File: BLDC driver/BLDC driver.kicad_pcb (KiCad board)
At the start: 4 copper layers, 75 x 50 mm, 41 parts, among them J1 Screw_Terminal_01x02, J2 Screw_Terminal_01x03, J3 Conn_02x06_Counter_Clockwise, J4 Izlaz ocitavanje struje, Q1 N0436N, Q2 N0436N, Q3 N0436N, Q4 N0436N, Q5 N0436N, Q6 N0436N, U1 MCP8027T-H/Y4X

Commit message: Ispravljene greske
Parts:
- moved J3 0.29 mm to (126.0, 74.1)
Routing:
- net PWM2L: track 15.5 -> 14.2 mm
- net I_OUT3: track 22.4 -> 23.3 mm
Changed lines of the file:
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@@
 			(at 3.75 -6.25 0)
 			(layer "F.SilkS")
+			(hide yes)
 			(effects
 				(font
@@
 			(at 3.75 6.25 0)
 			(layer "F.Fab")
+			(hide yes)
 			(effects
 				(font
@@
 	(footprint "Connector_PinHeader_2.54mm:PinHeader_2x06_P2.54mm_Vertical"
 		(layer "F.Cu")
-		(at 125.71 74.13)
+		(at 126 74.126511)
 		(descr "Through hole straight pin header, 2x06, 2.54mm pitch, double rows")
 		(tags "Through hole pin header THT 2x06 2.54mm double row")
@@
 			(at 1.27 -2.38 0)
 			(layer "F.SilkS")
+			(hide yes)
 			(effects
 				(font
@@
 			(at 1.27 15.08 0)
 			(layer "F.Fab")
+			(hide yes)
 			(effects
 				(font
@@
 	)
 	(segment
-		(start 128.25 81)
-		(end 132.314799 76.935201)
+		(start 129.691 80.595511)
+		(end 129.691 79.342479)
 		(width 0.2)
 		(layer "In2.Cu")
@@
 	)
 	(segment
-		(start 128.25 81.75)
-		(end 128.25 81)
+		(start 129.691 79.342479)
+		(end 132.314799 76.71868)
 		(width 0.2)
 		(layer "In2.Cu")
@@
 	)
 	(segment
+		(start 128.54 81.746511)
+		(end 128.387228 81.746511)
+		(width 0.2)
+		(layer "In2.Cu")
+		(net 36)
+	)
+	(segment
+		(start 128.387228 81.746511)
+		(end 128.25 81.609283)
+		(width 0.2)
+		(layer "In2.Cu")
+		(net 36)
+	)
+	(segment
+		(start 128.54 81.746511)
+		(end 129.691 80.595511)
+		(width 0.2)
+		(layer "In2.Cu")
+		(net 36)
+	)
+	(segment
 		(start 133 82.3375)
 		(end 133.4125 82.3375)
@@
 	)
 	(segment
-		(start 125.71 81.75)
-		(end 126.861 80.599)
+		(start 128.182489 77.817511)
+		(end 130.366025 77.817511)
 		(width 0.2)
 		(layer "In2.Cu")
@@
 	)
 	(segment
-		(start 126.861 78.97124)
-		(end 128.01124 77.821)
+		(start 127.389 78.611)
+		(end 128.182489 77.817511)
 		(width 0.2)
 		(layer "In2.Cu")
@@
 	)
 	(segment
-		(start 130.362536 77.821)
-		(end 136.082536 72.101)
+		(start 126 81.746511)
+		(end 127.389 80.357511)
 		(width 0.2)
 		(layer "In2.Cu")
@@
 	)
 	(segment
-		(start 128.01124 77.821)
-		(end 130.362536 77.821)
+		(start 136.082536 72.101)
+		(end 139.899 72.101)
 		(width 0.2)
 		(layer "In2.Cu")
@@
 	)
 	(segment
-		(start 126.861 80.599)
-		(end 126.861 78.97124)
+		(start 126 81.746511)
+		(end 126 81.46)
 		(width 0.2)
 		(layer "In2.Cu")
@@
 	)
 	(segment
-		(start 136.082536 72.101)
-		(end 139.899 72.101)
+		(start 127.389 80.357511)
+		(end 127.389 78.611)
+		(width 0.2)
+		(layer "In2.Cu")
+		(net 38)
+	)
+	(segment
+		(start 130.366025 77.817511)
+		(end 136.082536 72.101)
 		(width 0.2)
 		(layer "In2.Cu")
@@
 	)
 	(segment
-		(start 132.883212 78.3375)
-		(end 132.883212 77.25)
+		(start 134.75 79.5)
+		(end 133.558212 79.5)
 		(width 0.2)
 		(layer "F.Cu")
@@
 	)
 	(segment
-		(start 134.75 79.5)
-		(end 133.558212 79.5)
+		(start 132.883212 78.825)
+		(end 132.883212 78.3375)
 		(width 0.2)
 		(layer "F.Cu")
@@
 	)
 	(segment
-		(start 132.883212 78.825)
-		(end 132.883212 78.3375)
+		(start 132.883212 78.3375)
+		(end 132.883212 77.866788)
+		(width 0.2)
+		(layer "F.Cu")
+		(net 43)
+	)
+	(segment
+		(start 132.883212 77.866788)
+		(end 133.5 77.25)
 		(width 0.2)
 		(layer "F.Cu")
@@
 	)
 	(via
-		(at 132.883212 77.25)
+		(at 133.5 77.25)
 		(size 0.6)
 		(drill 0.3)
@@
 	)
 	(segment
+		(start 133.5 77.25)
+		(end 132.633212 77.25)
+		(width 0.2)
+		(layer "In2.Cu")
+		(net 43)
+	)
+	(segment
 		(start 132.633212 77.25)
 		(end 130.649 79.234212)
@@
 	)
 	(segment
-		(start 132.883212 77.25)
-		(end 132.633212 77.25)
+		(start 128.387228 74.126511)
+		(end 128.25 73.989283)
 		(width 0.2)
-		(layer "In2.Cu")
-		(net 43)
+		(layer "F.Cu")
+		(net 45)
 	)
 	(segment
-		(start 128.25 72.5)
-		(end 129.349 71.401)
+		(start 128.25 73.989283)
+		(end 128.25 72.5)
 		(width 0.2)
 		(layer "F.Cu")
@@
 	)
 	(segment
-		(start 137.1625 72.950376)
-		(end 137.1625 74.0875)
+		(start 128.25 72.5)
+		(end 129.349 71.401)
 		(width 0.2)
 		(layer "F.Cu")
@@
 	)
 	(segment
-		(start 128.25 74.13)
-		(end 128.25 72.5)
+		(start 129.349 71.401)
+		(end 135.613124 71.401)
 		(width 0.2)
 		(layer "F.Cu")
@@
 	)
 	(segment
-		(start 129.349 71.401)
-		(end 135.613124 71.401)
+		(start 128.54 74.126511)
+		(end 128.387228 74.126511)
+		(width 0.2)
+		(layer "F.Cu")
+		(net 45)
+	)
+	(segment
+		(start 137.1625 72.950376)
+		(end 137.1625 74.0875)
 		(width 0.2)
 		(layer "F.Cu")
@@
 	)
 	(segment
+		(start 128.54 76.38)
+		(end 128.54 76.666511)
+		(width 0.2)
+		(layer "F.Cu")
+		(net 46)
+	)
+	(segment
 		(start 130.8325 74.0875)
-		(end 128.25 76.67)
+		(end 128.54 76.38)
 		(width 0.2)
 		(layer "F.Cu")
@@
 	)
 	(segment
-		(start 128.25 79.169366)
-		(end 131.419366 76)
+		(start 128.54 79.206511)
+		(end 128.387228 79.053739)
+		(width 0.2)
+		(layer "F.Cu")
+		(net 47)
+	)
+	(segment
+		(start 128.387228 79.053739)
+		(end 128.387228 79.032138)
 		(width 0.2)
 		(layer "F.Cu")
@@
 	)
 	(segment
-		(start 128.25 79.21)
-		(end 128.25 79.169366)
+		(start 128.387228 79.032138)
+		(end 131.419366 76)
 		(width 0.2)
 		(layer "F.Cu")
@@
 	)
 	(segment
-		(start 130.698 71.802)
-		(end 135.246324 71.802)
+		(start 136.6625 73.218176)
+		(end 136.6625 74.0875)
 		(width 0.2)
 		(layer "F.Cu")
@@
 	)
 	(segment
-		(start 135.246324 71.802)
-		(end 136.6625 73.218176)
+		(start 133 71.802)
+		(end 135.246324 71.802)
 		(width 0.2)
 		(layer "F.Cu")
@@
 	)
 	(segment
-		(start 136.6625 73.218176)
-		(end 136.6625 74.0875)
+		(start 127 75.5)
+		(end 128.8529 75.5)
 		(width 0.2)
 		(layer "F.Cu")
@@
 	)
 	(segment
-		(start 128.8529 75.5)
-		(end 129.5 74.8529)
+		(start 132.5509 71.802)
+		(end 133 71.802)
 		(width 0.2)
 		(layer "F.Cu")
@@
 	)
 	(segment
-		(start 125.83 76.67)
-		(end 127 75.5)
+		(start 135.246324 71.802)
+		(end 136.6625 73.218176)
 		(width 0.2)
 		(layer "F.Cu")
@@
 	)
 	(segment
-		(start 127 75.5)
-		(end 128.8529 75.5)
+		(start 126 76.5)
+		(end 127 75.5)
 		(width 0.2)
 		(layer "F.Cu")
@@
 	)
 	(segment
-		(start 129.5 74.8529)
-		(end 129.5 73)
+		(start 126 76.666511)
+		(end 126 76.5)
 		(width 0.2)
 		(layer "F.Cu")
@@
 	)
 	(segment
-		(start 125.71 76.67)
-		(end 125.83 76.67)
+		(start 128.8529 75.5)
+		(end 132.5509 71.802)
 		(width 0.2)
 		(layer "F.Cu")
@@
 	)
 	(segment
-		(start 129.5 73)
-		(end 130.698 71.802)
+		(start 126 78.92)
+		(end 126 79.206511)
 		(width 0.2)
 		(layer "F.Cu")
-		(net 49)
+		(net 50)
 	)
 	(segment
-		(start 128.54776 78)
-		(end 126.92 78)
+		(start 134.75 75.5)
+		(end 131.352266 75.5)
 		(width 0.2)
 		(layer "F.Cu")
@@
 	)
 	(segment
-		(start 126.92 78)
-		(end 125.71 79.21)
+		(start 131.352266 75.5)
+		(end 128.852266 78)
 		(width 0.2)
 		(layer "F.Cu")
@@
 	)
 	(segment
-		(start 134.75 75.5)
-		(end 131.04776 75.5)
+		(start 126.92 78)
+		(end 126 78.92)
 		(width 0.2)
 		(layer "F.Cu")
@@
 	)
 	(segment
-		(start 131.04776 75.5)
-		(end 128.54776 78)
+		(start 128.852266 78)
+		(end 126.92 78)
 		(width 0.2)
 		(layer "F.Cu")
@@
 	)
 	(segment
-		(start 137.5 71.5)
-		(end 137.5 75.04)
+		(start 137.5 75.04)
+		(end 128.54 84)
 		(width 0.2)
 		(layer "B.Cu")
@@
 	)
 	(segment
-		(start 137.5 75.04)
-		(end 128.25 84.29)
+		(start 128.54 84)
+		(end 128.54 84.286511)
+		(width 0.2)
+		(layer "B.Cu")
+		(net 51)
+	)
+	(segment
+		(start 137.5 71.5)
+		(end 137.5 75.04)
 		(width 0.2)
 		(layer "B.Cu")
@@
 	)
 	(segment
+		(start 137.5 85.5)
+		(end 126.92 85.5)
+		(width 0.2)
+		(layer "B.Cu")
+		(net 52)
+	)
+	(segment
 		(start 126.92 85.5)
-		(end 125.71 84.29)
+		(end 126 84.58)
 		(width 0.2)
 		(layer "B.Cu")
@@
 	)
 	(segment
-		(start 137.5 85.5)
-		(end 126.92 85.5)
+		(start 126 84.58)
+		(end 126 84.286511)
 		(width 0.2)
 		(layer "B.Cu")

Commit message: Male ispravke
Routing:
- net PWM3H: track 13.0 -> 10.4 mm
- net PWM2L: track 14.2 -> 13.2 mm
- net PWM3L: track 14.7 -> 13.8 mm
- net 3V3: track 21.5 -> 20.8 mm
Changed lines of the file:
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@@
 	)
 	(segment
-		(start 140.1625 73.058771)
-		(end 140.1625 74.0875)
-		(width 0.2)
-		(layer "F.Cu")
-		(net 38)
-	)
-	(segment
-		(start 140 72)
-		(end 140 72.896271)
-		(width 0.2)
-		(layer "F.Cu")
-		(net 38)
-	)
-	(segment
-		(start 140 72.896271)
-		(end 140.1625 73.058771)
+		(start 140.1625 72.6625)
+		(end 140 72.5)
+		(width 0.2)
+		(layer "F.Cu")
+		(net 38)
+	)
+	(segment
+		(start 140.1625 74.0875)
+		(end 140.1625 72.6625)
 		(width 0.2)
 		(layer "F.Cu")
@@
 	)
 	(via
-		(at 140 72)
+		(at 140 72.5)
 		(size 0.6)
 		(drill 0.3)
@@
 	)
 	(segment
+		(start 127.389 80.357511)
+		(end 126 81.746511)
+		(width 0.2)
+		(layer "In2.Cu")
+		(net 38)
+	)
+	(segment
 		(start 128.182489 77.817511)
-		(end 130.366025 77.817511)
-		(width 0.2)
-		(layer "In2.Cu")
-		(net 38)
-	)
-	(segment
-		(start 127.389 78.611)
+		(end 127.389 78.611)
+		(width 0.2)
+		(layer "In2.Cu")
+		(net 38)
+	)
+	(segment
+		(start 130.366025 77.817511)
 		(end 128.182489 77.817511)
 		(width 0.2)
@@
 	)
 	(segment
-		(start 126 81.746511)
-		(end 127.389 80.357511)
-		(width 0.2)
-		(layer "In2.Cu")
-		(net 38)
-	)
-	(segment
-		(start 136.082536 72.101)
-		(end 139.899 72.101)
+		(start 130.366025 77.817511)
+		(end 135.683536 72.5)
+		(width 0.2)
+		(layer "In2.Cu")
+		(net 38)
+	)
+	(segment
+		(start 135.683536 72.5)
+		(end 140 72.5)
 		(width 0.2)
 		(layer "In2.Cu")
@@
 	)
 	(segment
-		(start 127.389 80.357511)
-		(end 127.389 78.611)
-		(width 0.2)
-		(layer "In2.Cu")
-		(net 38)
-	)
-	(segment
-		(start 130.366025 77.817511)
-		(end 136.082536 72.101)
-		(width 0.2)
-		(layer "In2.Cu")
-		(net 38)
-	)
-	(segment
-		(start 139.899 72.101)
-		(end 140 72)
+		(start 127.389 78.611)
+		(end 127.389 80.357511)
 		(width 0.2)
 		(layer "In2.Cu")
@@
 	)
 	(segment
-		(start 128.387228 74.126511)
-		(end 128.25 73.989283)
+		(start 130.067511 72.599)
+		(end 128.54 74.126511)
 		(width 0.2)
 		(layer "F.Cu")
@@
 	)
 	(segment
-		(start 128.25 73.989283)
-		(end 128.25 72.5)
+		(start 137.1625 73.151076)
+		(end 136.610424 72.599)
 		(width 0.2)
 		(layer "F.Cu")
@@
 	)
 	(segment
-		(start 135.613124 71.401)
-		(end 137.1625 72.950376)
+		(start 136.610424 72.599)
+		(end 130.067511 72.599)
 		(width 0.2)
 		(layer "F.Cu")
@@
 	)
 	(segment
-		(start 128.25 72.5)
-		(end 129.349 71.401)
-		(width 0.2)
-		(layer "F.Cu")
-		(net 45)
-	)
-	(segment
-		(start 129.349 71.401)
-		(end 135.613124 71.401)
-		(width 0.2)
-		(layer "F.Cu")
-		(net 45)
-	)
-	(segment
-		(start 128.54 74.126511)
-		(end 128.387228 74.126511)
-		(width 0.2)
-		(layer "F.Cu")
-		(net 45)
-	)
-	(segment
-		(start 137.1625 72.950376)
-		(end 137.1625 74.0875)
+		(start 137.1625 74.0875)
+		(end 137.1625 73.151076)
 		(width 0.2)
 		(layer "F.Cu")
@@
 	)
 	(segment
-		(start 129.172607 71)
-		(end 126.15826 74.014347)
+		(start 126 74.126511)
+		(end 127.928511 72.198)
 		(width 0.2)
 		(layer "F.Cu")
@@
 	)
 	(segment
-		(start 135.779224 71)
-		(end 129.172607 71)
+		(start 136.776524 72.198)
+		(end 137.6625 73.083976)
 		(width 0.2)
 		(layer "F.Cu")
@@
 	)
 	(segment
-		(start 137.6625 72.883276)
-		(end 135.779224 71)
+		(start 137.6625 73.083976)
+		(end 137.6625 74.0875)
 		(width 0.2)
 		(layer "F.Cu")
@@
 	)
 	(segment
-		(start 137.6625 74.0875)
-		(end 137.6625 72.883276)
+		(start 127.928511 72.198)
+		(end 136.776524 72.198)
 		(width 0.2)
 		(layer "F.Cu")
@@
 	)
 	(segment
-		(start 133 71.802)
-		(end 135.246324 71.802)
+		(start 126 76.666511)
+		(end 126 76.5)
 		(width 0.2)
 		(layer "F.Cu")
@@
 	)
 	(segment
-		(start 132.5509 71.802)
-		(end 133 71.802)
-		(width 0.2)
-		(layer "F.Cu")
-		(net 49)
-	)
-	(segment
-		(start 135.246324 71.802)
+		(start 136.444324 73)
 		(end 136.6625 73.218176)
+		(width 0.2)
+		(layer "F.Cu")
+		(net 49)
+	)
+	(segment
+		(start 128.8529 75.5)
+		(end 131.3529 73)
 		(width 0.2)
 		(layer "F.Cu")
@@
 	)
 	(segment
-		(start 126 76.666511)
-		(end 126 76.5)
-		(width 0.2)
-		(layer "F.Cu")
-		(net 49)
-	)
-	(segment
-		(start 128.8529 75.5)
-		(end 132.5509 71.802)
-		(width 0.2)
-		(layer "F.Cu")
+		(start 131.3529 73)
+		(end 136.444324 73)
+		(width 0.2)
+		(layer "F.Cu")

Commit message: Novi shunt-ovi
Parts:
- R1, R2, R3: value 0.01 -> WSLP2512R0100FEA; footprint Resistor_SMD:R_Shunt_Vishay_WSR2_WSR3_KelvinConnection -> Resistor_SMD:R_2512_6332Metric_Pad1.40x3.35mm_HandSolder
- R18, R4, R5, R6, R7, R8: value R_US -> 20
- moved R1 0.25 mm to (160.0, 98.2)
- moved R2 0.25 mm to (170.0, 98.2)
- moved R3 0.25 mm to (180.0, 98.2)
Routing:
- net Net-(Q5-S): track 35.3 -> 38.8 mm
- net GND: track 154.8 -> 156.0 mm
- net Net-(Q6-S): track 42.1 -> 42.7 mm

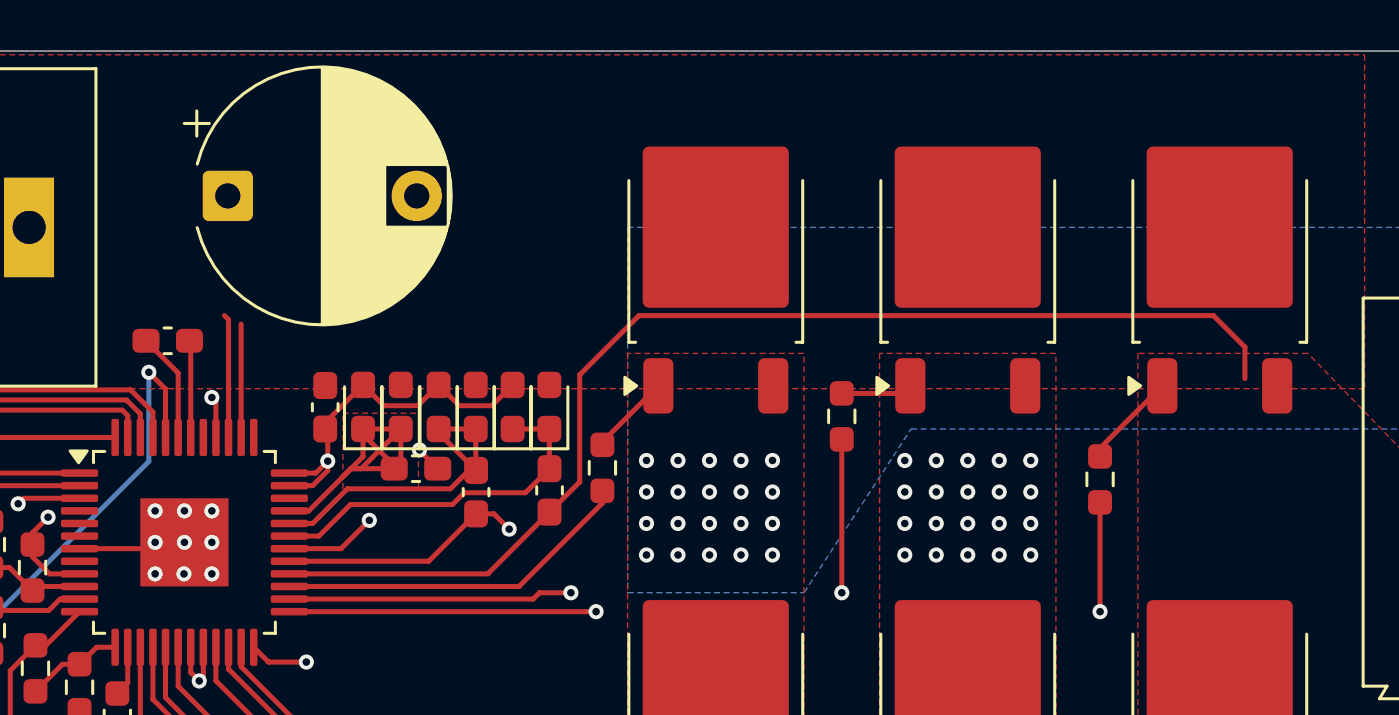
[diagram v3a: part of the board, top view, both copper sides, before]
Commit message: Promenjene diode usled greske
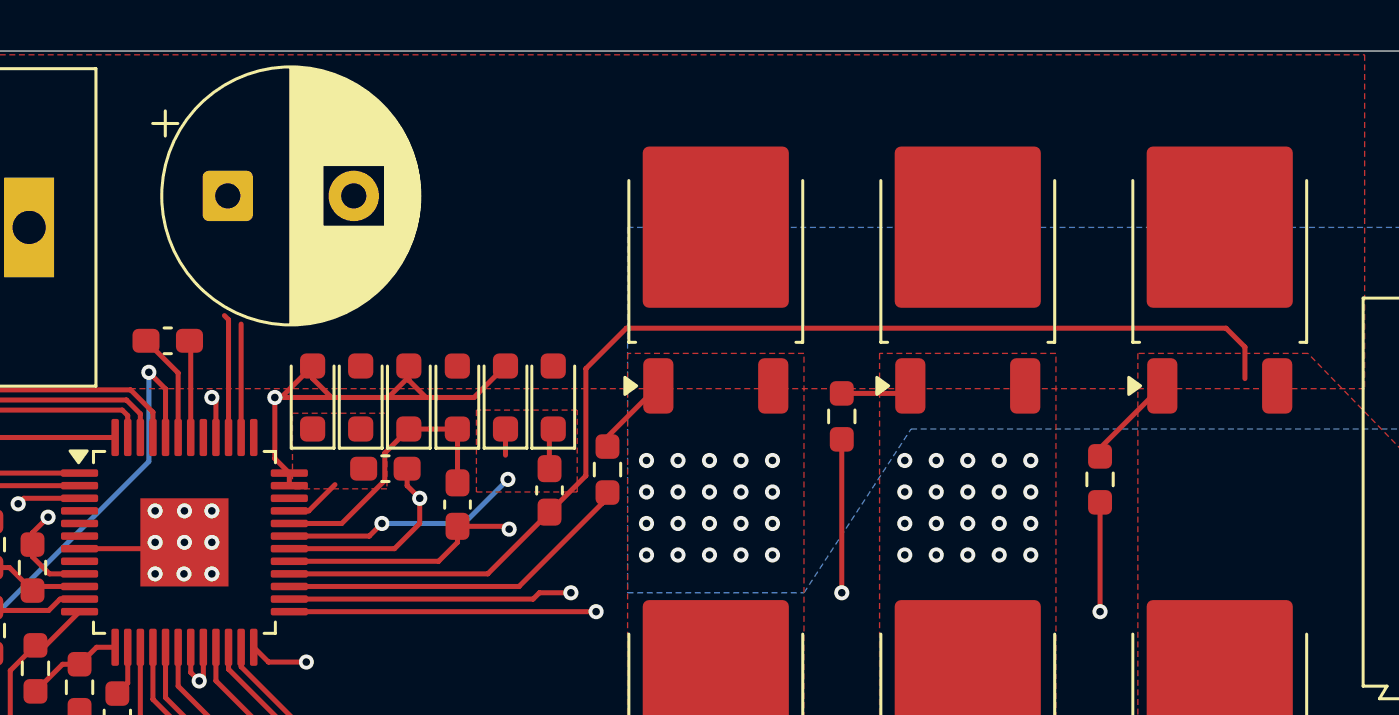
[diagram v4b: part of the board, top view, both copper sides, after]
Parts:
- removed C6: 470n, Capacitor_SMD:C_0603_1608Metric_Pad1.08x0.95mm_HandSolder
- C5: footprint Capacitor_THT:CP_Radial_D10.0mm_P7.50mm -> Capacitor_THT:CP_Radial_D10.0mm_P5.00mm
- D1, D2, D3, D4, D5, D6: value 1N5819 -> 1N5819WS; footprint Diode_SMD:D_0603_1608Metric_Pad1.05x0.95mm_HandSolder -> Diode_SMD:D_SOD-323_HandSoldering
- moved D6 2.03 mm to (144.0, 72.5)
- moved D1 1.64 mm to (145.9, 72.5)
- moved D5 1.24 mm to (147.8, 72.5)
- moved C3 1.21 mm to (146.9, 75.3)
- moved C1 0.89 mm to (149.8, 76.8)
- moved D2 0.82 mm to (149.7, 72.5)
- moved D4 0.47 mm to (151.7, 72.5)
- moved D3 0.41 mm to (153.5, 72.5)
- moved R4 0.21 mm to (155.7, 75.4)
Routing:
- net Net-(D1-K): track 15.6 -> 2.24 mm
- net Net-(J2-Pin_1): track 23.1 -> 17.3 mm, vias 22 -> 21
- net GND: track 156.0 -> 161.4 mm
- net Net-(D2-K): track 13.7 -> 11.0 mm
- net Net-(D3-K): track 14.5 -> 12.2 mm, vias 0 -> 2
- added copper zone on F.Cu, net Net-(D3-K)

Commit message: Dodadi kondenzatori, vratiti u slucaju greske
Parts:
- added C10: 470n, Capacitor_SMD:C_0603_1608Metric_Pad1.08x0.95mm_HandSolder, F.Cu at (160.5, 62.2)
- added C11: 470n, Capacitor_SMD:C_0603_1608Metric_Pad1.08x0.95mm_HandSolder, F.Cu at (162.0, 62.2)
- added C12: 470n, Capacitor_SMD:C_0603_1608Metric_Pad1.08x0.95mm_HandSolder, F.Cu at (163.5, 62.2)
- added C13: 470n, Capacitor_SMD:C_0603_1608Metric_Pad1.08x0.95mm_HandSolder, F.Cu at (166.0, 62.2)
- added C14: 470n, Capacitor_SMD:C_0603_1608Metric_Pad1.08x0.95mm_HandSolder, F.Cu at (167.5, 62.2)
- added C15: 470n, Capacitor_SMD:C_0603_1608Metric_Pad1.08x0.95mm_HandSolder, F.Cu at (169.0, 62.2)
- added C16: 470n, Capacitor_SMD:C_0603_1608Metric_Pad1.08x0.95mm_HandSolder, F.Cu at (170.5, 62.2)
- added C17: 470n, Capacitor_SMD:C_0603_1608Metric_Pad1.08x0.95mm_HandSolder, F.Cu at (172.0, 62.2)
- added C18: 470n, Capacitor_SMD:C_0603_1608Metric_Pad1.08x0.95mm_HandSolder, F.Cu at (173.5, 62.2)
- added C19: 470n, Capacitor_SMD:C_0603_1608Metric_Pad1.08x0.95mm_HandSolder, F.Cu at (182.0, 62.2)
- added C20: 470n, Capacitor_SMD:C_0603_1608Metric_Pad1.08x0.95mm_HandSolder, F.Cu at (183.5, 62.2)
- added C21: 470n, Capacitor_SMD:C_0603_1608Metric_Pad1.08x0.95mm_HandSolder, F.Cu at (176.0, 62.2)
- added C22: 470n, Capacitor_SMD:C_0603_1608Metric_Pad1.08x0.95mm_HandSolder, F.Cu at (177.5, 62.2)
- added C23: 470n, Capacitor_SMD:C_0603_1608Metric_Pad1.08x0.95mm_HandSolder, F.Cu at (179.0, 62.2)
- added C24: 470n, Capacitor_SMD:C_0603_1608Metric_Pad1.08x0.95mm_HandSolder, F.Cu at (180.5, 62.2)
- added C6: 470n, Capacitor_SMD:C_0603_1608Metric_Pad1.08x0.95mm_HandSolder, F.Cu at (141.1, 73.5)
- added C7: 470n, Capacitor_SMD:C_0603_1608Metric_Pad1.08x0.95mm_HandSolder, F.Cu at (156.0, 62.2)
- added C8: 470n, Capacitor_SMD:C_0603_1608Metric_Pad1.08x0.95mm_HandSolder, F.Cu at (157.5, 62.2)
- added C9: 470n, Capacitor_SMD:C_0603_1608Metric_Pad1.08x0.95mm_HandSolder, F.Cu at (159.0, 62.2)
- added H1: MountingHole, MountingHole:MountingHole_3.2mm_M3, F.Cu at (127.5, 62.2)
- added H2: MountingHole, MountingHole:MountingHole_3.2mm_M3, F.Cu at (195.5, 62.2)
- added H3: MountingHole, MountingHole:MountingHole_3.2mm_M3, F.Cu at (195.5, 105.2)
- added H4: MountingHole, MountingHole:MountingHole_3.2mm_M3, F.Cu at (127.5, 105.2)
- moved J1 18.8 mm to (151.5, 65.2)
- moved C5 6.14 mm to (134.5, 64.8)
- moved R5 4.01 mm to (164.7, 77.2)
- moved R11 3.01 mm to (131.0, 84.8)
- moved R13 3.01 mm to (131.0, 81.3)
- moved C4 2.37 mm to (137.5, 72.5)
- moved J3 1.75 mm to (125.9, 75.9)
- moved D2 1.73 mm to (149.5, 74.2)
- moved J2 1.73 mm to (191.7, 72.9)
- moved R12 1.73 mm to (141.4, 89.6)
- moved R14 1.73 mm to (139.9, 91.1)
- moved R4 1.73 mm to (155.4, 77.1)
- moved R9 1.73 mm to (136.0, 86.9)
- moved C1 1.73 mm to (149.5, 78.5)
- moved C2 1.73 mm to (153.1, 77.9)
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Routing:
- net GND: track 161.4 -> 166.1 mm, vias 42 -> 64
- net Net-(U1-HSB): track 28.1 -> 25.8 mm
- net Net-(D1-K): track 2.24 -> 3.93 mm
- net unconnected-(U1-+12V-Pad34): track 0.00 -> 1.67 mm
- net Net-(Q2-G): track 3.37 -> 4.35 mm
- net PWM2H: track 8.86 -> 7.93 mm
- net Net-(Q4-S): track 31.0 -> 31.8 mm
- net DE2: track 19.4 -> 18.7 mm
- net PWM1H: track 7.86 -> 7.25 mm
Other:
- outline, holes or cut-outs redrawn
